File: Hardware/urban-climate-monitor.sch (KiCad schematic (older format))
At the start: 35 parts, among them J1 Conn_ARM_JTAG_SWD_10, U1 AAT1217, U2 TPS27081A, U3 SHT30-DIS, U4 TSD305, U5 TSV911RILT, U6 RFM95W, U7 STM32L412KB

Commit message: Update prototype pin assignment
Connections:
- net labels added: RFM95_IRQ
- no-connect marks 12 -> 11
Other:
- moved on the sheet: C8
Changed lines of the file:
@@
 Text GLabel 2400 2250 0    50   Input ~ 0
 SHT30_NRST
-$Comp
-L my-symbols-library:RFM95W U6
-U 1 1 5F98AF14
-P 3150 5600
-F 0 "U6" H 3150 6215 50  0000 C CNN
-F 1 "RFM95W" H 3150 6124 50  0000 C CNN
-F 2 "" H 3150 5100 50  0001 C CNN
-F 3 "" H 3150 5100 50  0001 C CNN
-	1    3150 5600
-	1    0    0    -1
-$EndComp
-$Comp
-L Device:C C8
-U 1 1 5F98D147
-P 4200 5800
-F 0 "C8" H 4315 5846 50  0000 L CNN
-F 1 "100nF" H 4315 5755 50  0000 L CNN
-F 2 "Capacitor_SMD:C_0805_2012Metric_Pad1.15x1.40mm_HandSolder" H 4238 5650 50  0001 C CNN
-F 3 "~" H 4200 5800 50  0001 C CNN
-	1    4200 5800
-	1    0    0    -1
-$EndComp
-$Comp
-L power:GND #PWR019
-U 1 1 5F992340
-P 2550 6250
-F 0 "#PWR019" H 2550 6000 50  0001 C CNN
-F 1 "GND" H 2555 6077 50  0000 C CNN
-F 2 "" H 2550 6250 50  0001 C CNN
-F 3 "" H 2550 6250 50  0001 C CNN
-	1    2550 6250
-	1    0    0    -1
-$EndComp
-$Comp
-L power:GND #PWR020
-U 1 1 5F9971A4
-P 3850 6250
-F 0 "#PWR020" H 3850 6000 50  0001 C CNN
-F 1 "GND" H 3855 6077 50  0000 C CNN
-F 2 "" H 3850 6250 50  0001 C CNN
-F 3 "" H 3850 6250 50  0001 C CNN
-	1    3850 6250
-	1    0    0    -1
-$EndComp
-$Comp
-L power:GND #PWR021
-U 1 1 5F99C085
-P 4200 6250
-F 0 "#PWR021" H 4200 6000 50  0001 C CNN
-F 1 "GND" H 4205 6077 50  0000 C CNN
-F 2 "" H 4200 6250 50  0001 C CNN
-F 3 "" H 4200 6250 50  0001 C CNN
-	1    4200 6250
-	1    0    0    -1
-$EndComp
-Wire Wire Line
-	2750 5250 2550 5250
-Wire Wire Line
-	2550 5250 2550 5950
-Wire Wire Line
-	2750 5950 2550 5950
-Connection ~ 2550 5950
-Wire Wire Line
-	2550 5950 2550 6250
-Wire Wire Line
-	3550 5850 3850 5850
-Wire Wire Line
-	3850 5850 3850 6250
-Wire Wire Line
-	3550 5550 4200 5550
-Wire Wire Line
-	4200 5550 4200 5650
-Wire Wire Line
-	4200 5950 4200 6250
-Wire Wire Line
-	3550 5250 3650 5250
-Wire Wire Line
-	3550 5350 3650 5350
-Wire Wire Line
-	3550 5450 3650 5450
-Wire Wire Line
-	3550 5650 3650 5650
-Wire Wire Line
-	3550 5750 3650 5750
-Wire Wire Line
-	2750 5850 2650 5850
-NoConn ~ 2650 5850
-Wire Wire Line
-	2450 5650 2750 5650
-Wire Wire Line
-	2050 5750 2750 5750
-Wire Wire Line
-	2450 5650 1950 5650
-Connection ~ 2450 5650
-Wire Wire Line
-	2050 5750 1950 5750
-Connection ~ 2050 5750
-$Comp
-L Device:R R4
-U 1 1 5FA4C619
-P 2450 4700
-F 0 "R4" H 2520 4746 50  0000 L CNN
-F 1 "100k" H 2520 4655 50  0000 L CNN
-F 2 "Resistor_SMD:R_0805_2012Metric_Pad1.15x1.40mm_HandSolder" V 2380 4700 50  0001 C CNN
-F 3 "~" H 2450 4700 50  0001 C CNN
-	1    2450 4700
-	1    0    0    -1
-$EndComp
-$Comp
-L Device:R R3
-U 1 1 5FA530B6
-P 2050 4700
-F 0 "R3" H 2120 4746 50  0000 L CNN
-F 1 "100k" H 2120 4655 50  0000 L CNN
-F 2 "Resistor_SMD:R_0805_2012Metric_Pad1.15x1.40mm_HandSolder" V 1980 4700 50  0001 C CNN
-F 3 "~" H 2050 4700 50  0001 C CNN
-	1    2050 4700
-	1    0    0    -1
-$EndComp
-Wire Wire Line
-	2450 4850 2450 5650
-Wire Wire Line
-	2050 4850 2050 5750
-$Comp
-L power:+3.3V #PWR015
-U 1 1 5FA8AEAD
-P 2050 4400
-F 0 "#PWR015" H 2050 4250 50  0001 C CNN
-F 1 "+3.3V" H 2065 4573 50  0000 C CNN
-F 2 "" H 2050 4400 50  0001 C CNN
-F 3 "" H 2050 4400 50  0001 C CNN
-	1    2050 4400
-	1    0    0    -1
-$EndComp
-Wire Wire Line
-	2050 4400 2050 4550
-$Comp
-L power:+3.3V #PWR016
-U 1 1 5FA91C0B
-P 2450 4400
-F 0 "#PWR016" H 2450 4250 50  0001 C CNN
-F 1 "+3.3V" H 2465 4573 50  0000 C CNN
-F 2 "" H 2450 4400 50  0001 C CNN
-F 3 "" H 2450 4400 50  0001 C CNN
-	1    2450 4400
-	1    0    0    -1
-$EndComp
-Wire Wire Line
-	2450 4400 2450 4550
-Wire Wire Line
-	1950 5550 2750 5550
-Wire Wire Line
-	1950 5350 2750 5350
-Wire Wire Line
-	1950 5450 2750 5450
-Text GLabel 1950 5350 0    50   Input ~ 0
-MISO
-Text GLabel 1950 5450 0    50   Input ~ 0
-MOSI
-Text GLabel 1950 5550 0    50   Input ~ 0
-SCK
-Text GLabel 1950 5650 0    50   Input ~ 0
-RFM95W_NSS
-Text GLabel 1950 5750 0    50   Input ~ 0
-RFM95W_RST
-NoConn ~ 3650 5750
-NoConn ~ 3650 5650
-NoConn ~ 3650 5450
-NoConn ~ 3650 5350
-NoConn ~ 3650 5250
-Text Notes 3800 6150 2    50   ~ 0
-TODO: ANTENNA
 Wire Wire Line
 	14400 1700 15150 1700
@@
 $EndComp
 $Comp
-L power:+3.3V #PWR017
-U 1 1 5F8F769A
-P 4200 4450
-F 0 "#PWR017" H 4200 4300 50  0001 C CNN
-F 1 "+3.3V" H 4215 4623 50  0000 C CNN
-F 2 "" H 4200 4450 50  0001 C CNN
-F 3 "" H 4200 4450 50  0001 C CNN
-	1    4200 4450
-	1    0    0    -1
-$EndComp
-Wire Wire Line
-	4200 4450 4200 5550
-Connection ~ 4200 5550
-$Comp
 L power:GND #PWR018
 U 1 1 5F8F70A4
@@
 Text Notes 8300 3850 0    50   ~ 0
 Light Sensor
+$Comp
+L power:+3.3V #PWR017
+U 1 1 5F8F769A
+P 4350 4450
+F 0 "#PWR017" H 4350 4300 50  0001 C CNN
+F 1 "+3.3V" H 4365 4623 50  0000 C CNN
+F 2 "" H 4350 4450 50  0001 C CNN
+F 3 "" H 4350 4450 50  0001 C CNN
+	1    4350 4450
+	1    0    0    -1
+$EndComp
+Wire Wire Line
+	4350 5950 4350 6250
+$Comp
+L power:GND #PWR021
+U 1 1 5F99C085
+P 4350 6250
+F 0 "#PWR021" H 4350 6000 50  0001 C CNN
+F 1 "GND" H 4355 6077 50  0000 C CNN
+F 2 "" H 4350 6250 50  0001 C CNN
+F 3 "" H 4350 6250 50  0001 C CNN
+	1    4350 6250
+	1    0    0    -1
+$EndComp
+$Comp
+L Device:C C8
+U 1 1 5F98D147
+P 4350 5800
+F 0 "C8" H 4465 5846 50  0000 L CNN
+F 1 "100nF" H 4465 5755 50  0000 L CNN
+F 2 "Capacitor_SMD:C_0805_2012Metric_Pad1.15x1.40mm_HandSolder" H 4388 5650 50  0001 C CNN
+F 3 "~" H 4350 5800 50  0001 C CNN
+	1    4350 5800
+	1    0    0    -1
+$EndComp
+Wire Wire Line
+	3850 5850 3850 6250
+$Comp
+L power:GND #PWR020
+U 1 1 5F9971A4
+P 3850 6250
+F 0 "#PWR020" H 3850 6000 50  0001 C CNN
+F 1 "GND" H 3855 6077 50  0000 C CNN
+F 2 "" H 3850 6250 50  0001 C CNN
+F 3 "" H 3850 6250 50  0001 C CNN
+	1    3850 6250
+	1    0    0    -1
+$EndComp
+Text Notes 3800 6150 2    50   ~ 0
+TODO: ANTENNA
+$Comp
+L power:GND #PWR019
+U 1 1 5F992340
+P 2550 6250
+F 0 "#PWR019" H 2550 6000 50  0001 C CNN
+F 1 "GND" H 2555 6077 50  0000 C CNN
+F 2 "" H 2550 6250 50  0001 C CNN
+F 3 "" H 2550 6250 50  0001 C CNN
+	1    2550 6250
+	1    0    0    -1
+$EndComp
+Text GLabel 1950 5750 0    50   Input ~ 0
+RFM95W_RST
+Text GLabel 1950 5650 0    50   Input ~ 0
+RFM95W_NSS
+Text GLabel 1950 5550 0    50   Input ~ 0
+SCK
+Text GLabel 1950 5450 0    50   Input ~ 0
+MOSI
+Text GLabel 1950 5350 0    50   Input ~ 0
+MISO
+Wire Wire Line
+	2450 4400 2450 4550
+$Comp
+L power:+3.3V #PWR016
+U 1 1 5FA91C0B
+P 2450 4400
+F 0 "#PWR016" H 2450 4250 50  0001 C CNN
+F 1 "+3.3V" H 2465 4573 50  0000 C CNN
+F 2 "" H 2450 4400 50  0001 C CNN
+F 3 "" H 2450 4400 50  0001 C CNN
+	1    2450 4400
+	1    0    0    -1
+$EndComp
+Wire Wire Line
+	2050 4400 2050 4550
+$Comp
+L power:+3.3V #PWR015
+U 1 1 5FA8AEAD
+P 2050 4400
+F 0 "#PWR015" H 2050 4250 50  0001 C CNN
+F 1 "+3.3V" H 2065 4573 50  0000 C CNN
+F 2 "" H 2050 4400 50  0001 C CNN
+F 3 "" H 2050 4400 50  0001 C CNN
+	1    2050 4400
+	1    0    0    -1
+$EndComp
+Wire Wire Line
+	2050 4850 2050 5750
+Wire Wire Line
+	2450 4850 2450 5650
+$Comp
+L Device:R R3
+U 1 1 5FA530B6
+P 2050 4700
+F 0 "R3" H 2120 4746 50  0000 L CNN
+F 1 "100k" H 2120 4655 50  0000 L CNN
+F 2 "Resistor_SMD:R_0805_2012Metric_Pad1.15x1.40mm_HandSolder" V 1980 4700 50  0001 C CNN
+F 3 "~" H 2050 4700 50  0001 C CNN
+	1    2050 4700
+	1    0    0    -1
+$EndComp
+$Comp
+L Device:R R4
+U 1 1 5FA4C619
+P 2450 4700
+F 0 "R4" H 2520 4746 50  0000 L CNN
+F 1 "100k" H 2520 4655 50  0000 L CNN
+F 2 "Resistor_SMD:R_0805_2012Metric_Pad1.15x1.40mm_HandSolder" V 2380 4700 50  0001 C CNN
+F 3 "~" H 2450 4700 50  0001 C CNN
+	1    2450 4700
+	1    0    0    -1
+$EndComp
+Wire Wire Line
+	2050 5750 1950 5750
+Wire Wire Line
+	2450 5650 1950 5650
+Wire Wire Line
+	3550 5850 3850 5850
+NoConn ~ 3650 5250
+NoConn ~ 3650 5350
+NoConn ~ 3650 5650
+NoConn ~ 3650 5750
+Wire Wire Line
+	3550 5750 3650 5750
+Wire Wire Line
+	3550 5650 3650 5650
+Wire Wire Line
+	3550 5450 3650 5450
+Wire Wire Line
+	3550 5350 3650 5350
+Wire Wire Line
+	3550 5250 3650 5250
+Wire Wire Line
+	4350 4450 4350 5550
+Wire Wire Line
+	4350 5550 4350 5650
+Connection ~ 4350 5550
+Wire Wire Line
+	3550 5550 4350 5550
+Wire Wire Line
+	1950 5450 2750 5450
+Wire Wire Line
+	1950 5350 2750 5350
+Wire Wire Line
+	1950 5550 2750 5550
+Connection ~ 2050 5750
+Wire Wire Line
+	2050 5750 2750 5750
+Connection ~ 2450 5650
+Wire Wire Line
+	2450 5650 2750 5650
+NoConn ~ 2650 5850
+Wire Wire Line
+	2750 5850 2650 5850
+Wire Wire Line
+	2550 5950 2550 6250
+Wire Wire Line
+	2750 5950 2550 5950
+Connection ~ 2550 5950
+Wire Wire Line
+	2550 5250 2550 5950
+Wire Wire Line
+	2750 5250 2550 5250
+$Comp
+L my-symbols-library:RFM95W U6
+U 1 1 5F98AF14
+P 3150 5600
+F 0 "U6" H 3150 6215 50  0000 C CNN
+F 1 "RFM95W" H 3150 6124 50  0000 C CNN
+F 2 "" H 3150 5100 50  0001 C CNN
+F 3 "" H 3150 5100 50  0001 C CNN
+	1    3150 5600
+	1    0    0    -1
+$EndComp
+Text GLabel 3650 5450 2    50   Input ~ 0
+RFM95_IRQ
 $EndSCHEMATC

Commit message: Remove rfm9x submodule, sht3x test in main application
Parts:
- removed U3: SHT30-DIS, Sensor_Humidity:Sensirion_DFN-8-1EP_2.5x2.5mm_P0.5mm_EP1.1x1.7mm, symbol Sensor_Humidity:SHT30-DIS
- added U?: SHT31-DIS, Sensor_Humidity:Sensirion_DFN-8-1EP_2.5x2.5mm_P0.5mm_EP1.1x1.7mm, symbol Sensor_Humidity:SHT31-DIS
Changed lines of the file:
@@
-$EndComp
-$Comp
-L Sensor_Humidity:SHT30-DIS U3
-U 1 1 5F8B7348
-P 3000 2250
-F 0 "U3" H 3350 2700 50  0000 C CNN
-F 1 "SHT30-DIS" H 3350 2600 50  0000 C CNN
-F 2 "Sensor_Humidity:Sensirion_DFN-8-1EP_2.5x2.5mm_P0.5mm_EP1.1x1.7mm" H 3000 2300 50  0001 C CNN
-F 3 "https://www.sensirion.com/fileadmin/user_upload/customers/sensirion/Dokumente/2_Humidity_Sensors/Datasheets/Sensirion_Humidity_Sensors_SHT3x_Datasheet_digital.pdf" H 3000 2300 50  0001 C CNN
-	1    3000 2250
-	1    0    0    -1
 $EndComp
 $Comp
@@
 Text GLabel 3650 5450 2    50   Input ~ 0
 RFM95_IRQ
+$Comp
+L Sensor_Humidity:SHT31-DIS U?
+U 1 1 5FAE73AC
+P 3000 2250
+F 0 "U?" H 3300 2650 50  0000 C CNN
+F 1 "SHT31-DIS" H 3300 2550 50  0000 C CNN
+F 2 "Sensor_Humidity:Sensirion_DFN-8-1EP_2.5x2.5mm_P0.5mm_EP1.1x1.7mm" H 3000 2300 50  0001 C CNN
+F 3 "https://www.sensirion.com/fileadmin/user_upload/customers/sensirion/Dokumente/2_Humidity_Sensors/Datasheets/Sensirion_Humidity_Sensors_SHT3x_Datasheet_digital.pdf" H 3000 2300 50  0001 C CNN
+	1    3000 2250
+	1    0    0    -1
+$EndComp
 $EndSCHEMATC

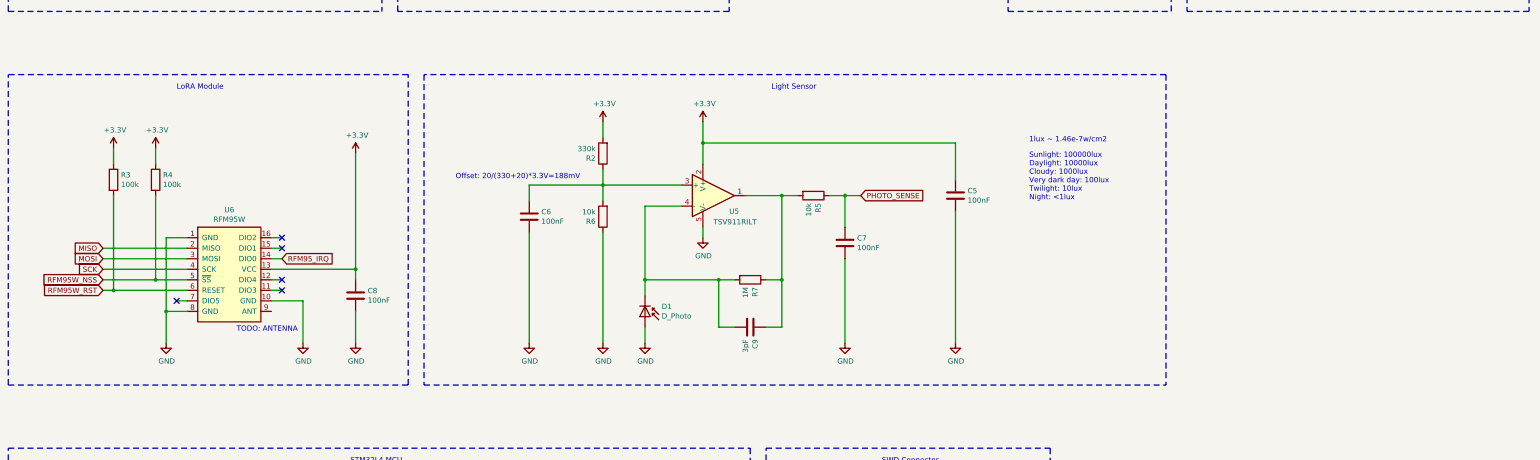
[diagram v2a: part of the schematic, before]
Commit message: Include EEPROM in schematic
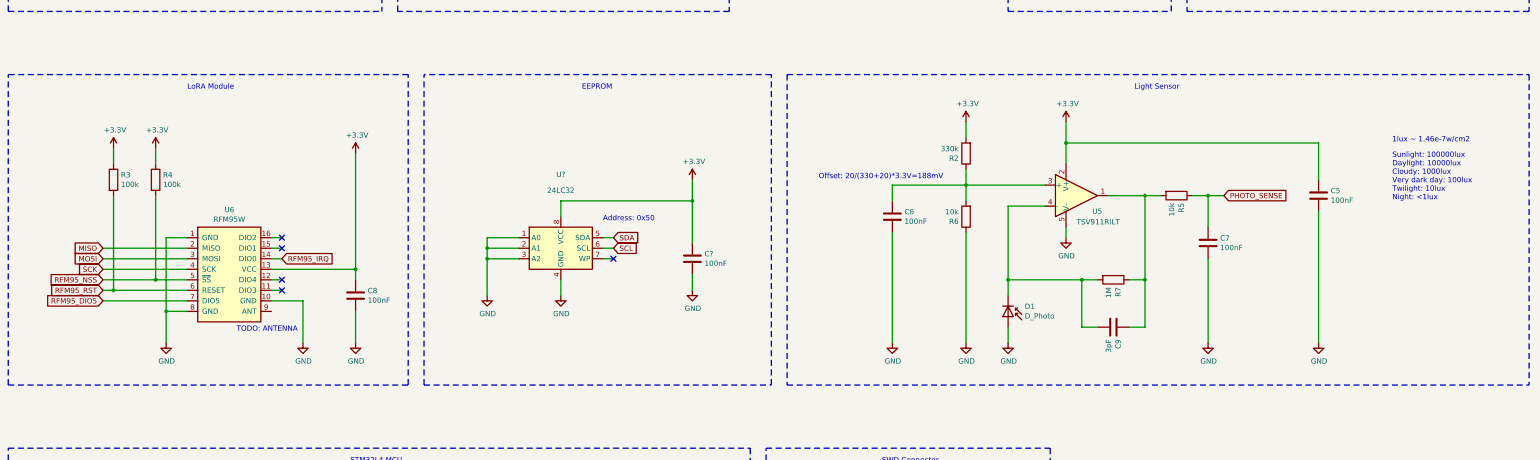
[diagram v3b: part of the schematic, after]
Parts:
- added C?: 100nF, Capacitor_SMD:C_0805_2012Metric_Pad1.15x1.40mm_HandSolder, symbol Device:C
- added U?: 24LC32, symbol Memory_EEPROM:24LC32
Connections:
- net labels added: RFM95_DIO5, RFM95_NSS, RFM95_RST
- net labels removed: RFM95W_NSS, RFM95W_RST
- wire segments 187 -> 202
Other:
- note added: "Address: 0x50"
- note added: "EEPROM"
- moved on the sheet: C5, C6, C7, C9, D1, R2, R5, R6, R7, U5

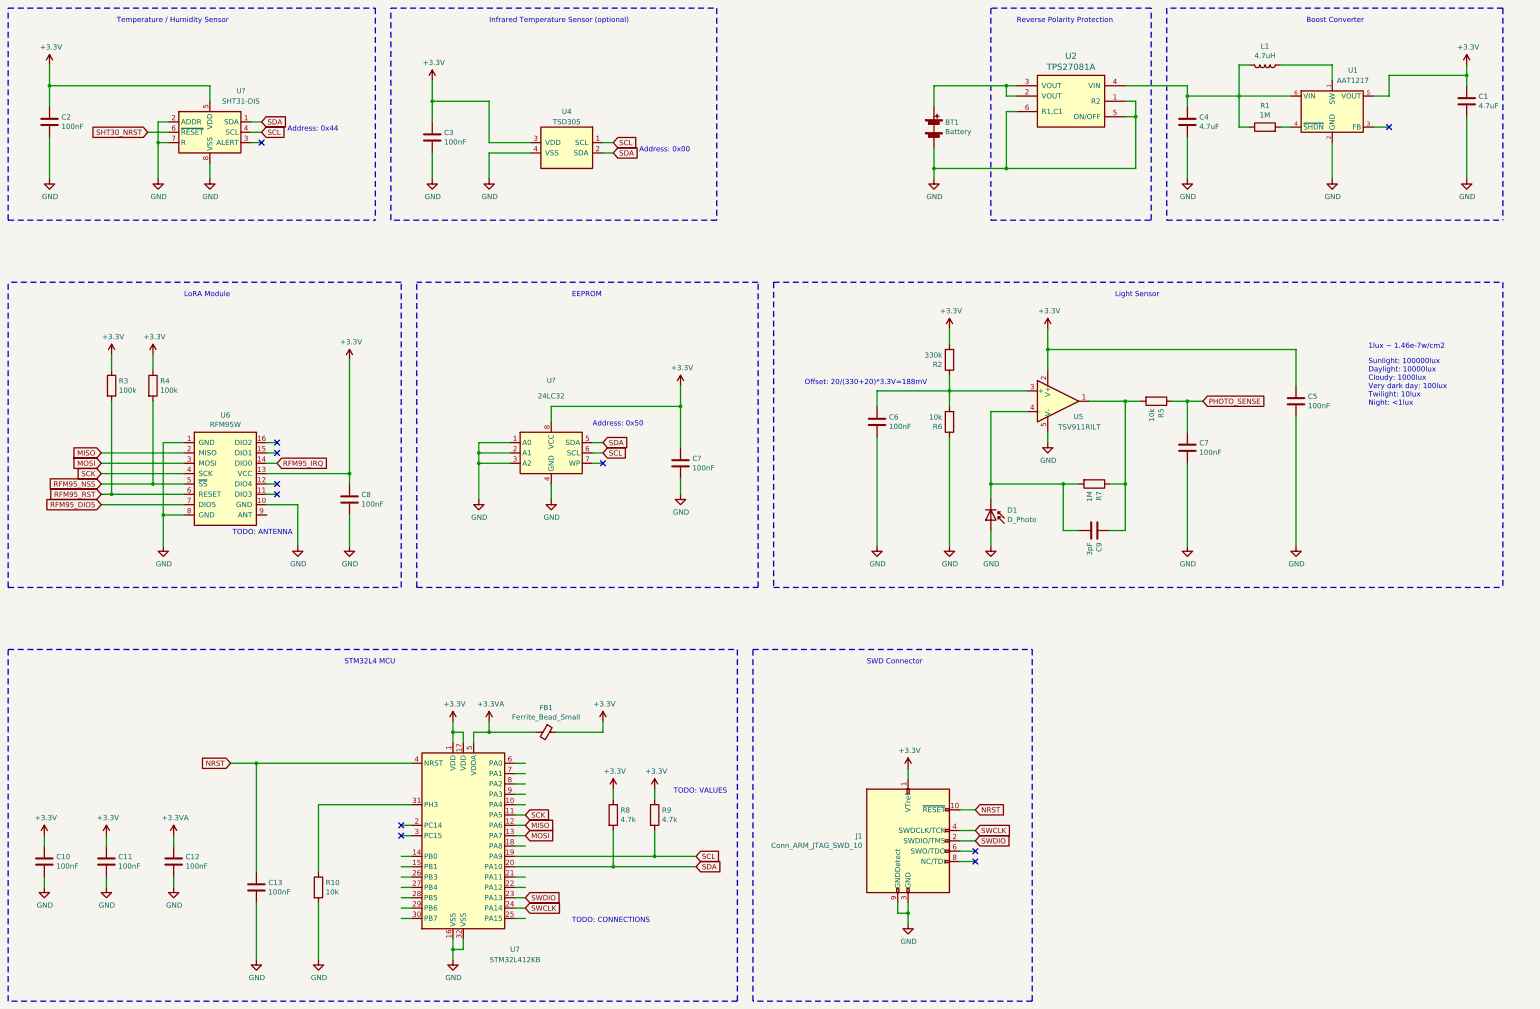
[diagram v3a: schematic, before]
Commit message: Add photo sensing implementation
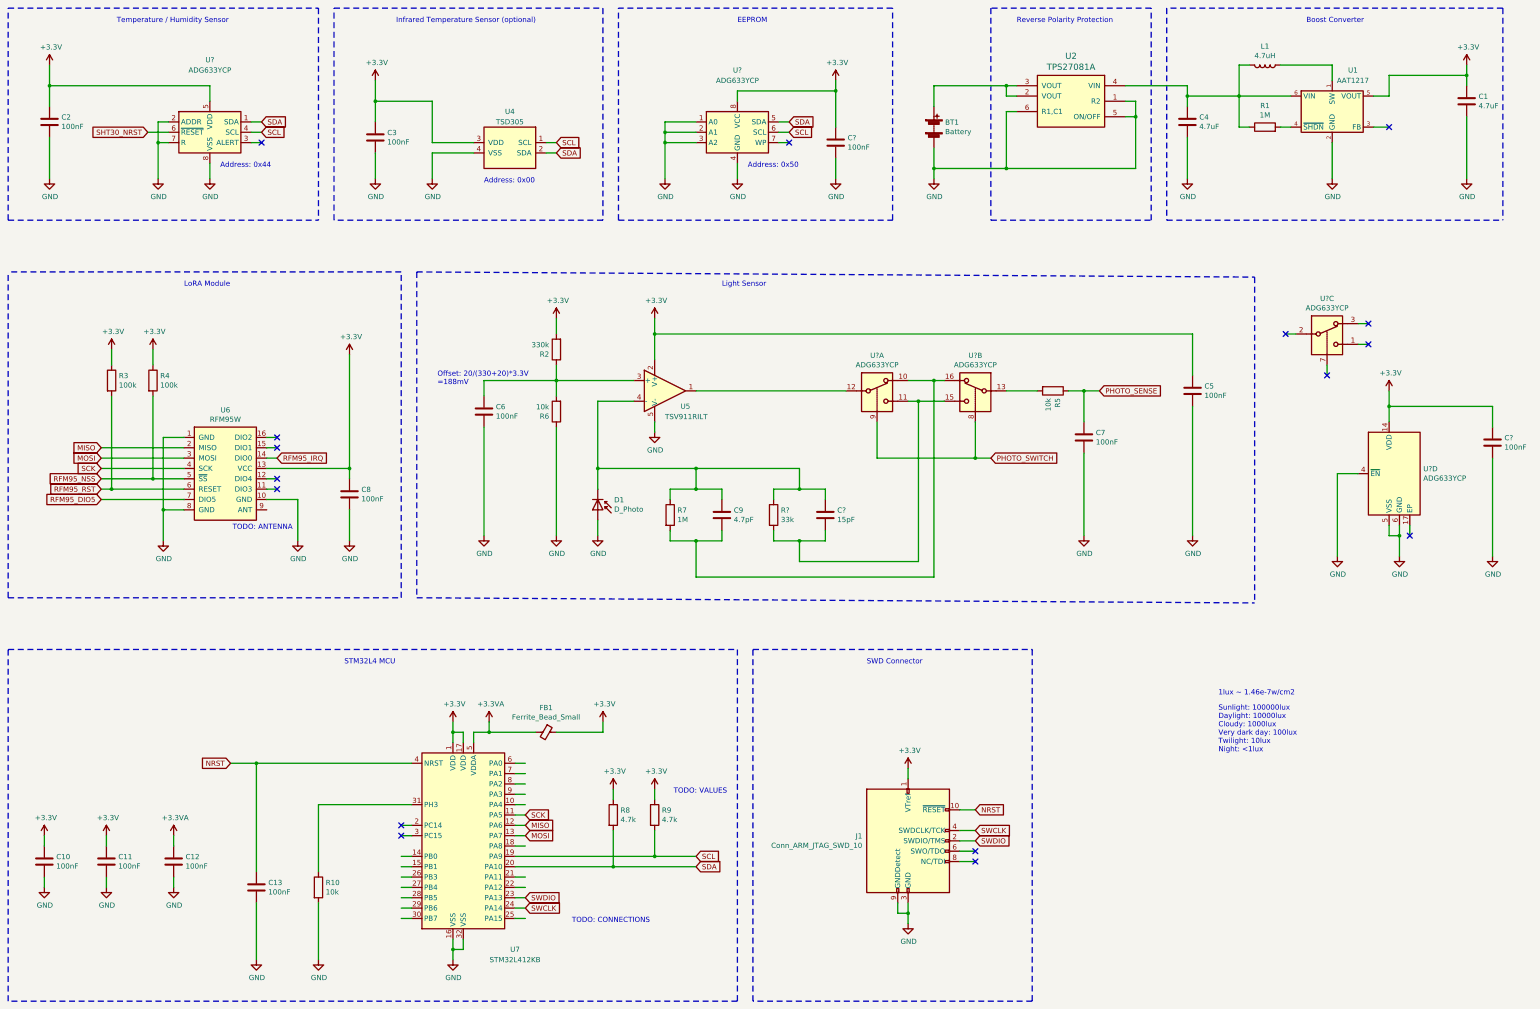
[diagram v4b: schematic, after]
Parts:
- added C?: 15pF, Capacitor_SMD:C_0805_2012Metric_Pad1.15x1.40mm_HandSolder, symbol Device:C
- added C?: 100nF, Capacitor_SMD:C_0805_2012Metric_Pad1.15x1.40mm_HandSolder, symbol Device:C
- added R?: 33k, Resistor_SMD:R_0805_2012Metric_Pad1.15x1.40mm_HandSolder, symbol Device:R
- added U? (x4): ADG633YCP, Package_CSP:LFCSP-16-1EP_4x4mm_P0.65mm_EP2.1x2.1mm, symbol Analog_Switch:ADG633YCP
- C9: value 3pF -> 4.7pF
- U?: value 24LC32 -> ADG633YCP; footprint (none) -> Package_CSP:LFCSP-16-1EP_4x4mm_P0.65mm_EP2.1x2.1mm
- U?: value SHT31-DIS -> ADG633YCP; footprint Sensor_Humidity:Sensirion_DFN-8-1EP_2.5x2.5mm_P0.5mm_EP1.1x1.7mm -> Package_CSP:LFCSP-16-1EP_4x4mm_P0.65mm_EP2.1x2.1mm
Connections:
- net labels added: PHOTO_SWITCH
- wire segments 202 -> 244
- no-connect marks 11 -> 16
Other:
- note added: "Offset: 20/(330+20)*3.3V\n=188mV"
- note removed: "Offset: 20/(330+20)*3.3V=188mV"
- moved on the sheet: C3, C5, C6, C7, C8, C9, C?, D1, R2, R3, R4, R5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
